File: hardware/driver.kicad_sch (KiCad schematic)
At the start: 33 parts, among them U4 EPC2152, U5 EPC2152, U6 INA181A2IDBVT, U7 INA181A2IDBVT, U8 EPC2152, U9 INA181A2IDBVT

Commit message: some layout
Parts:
- gave numbers to parts that had none: 12
- renumbered C22 to C42, C23 to C43, C24 to C44, C25 to C45, C26 to C46, C27 to C47, C28 to C48, C29 to C49, C30 to C50, R11 to R15, R12 to R16, R13 to R17, R14 to R18, R15 to R19, R16 to R23

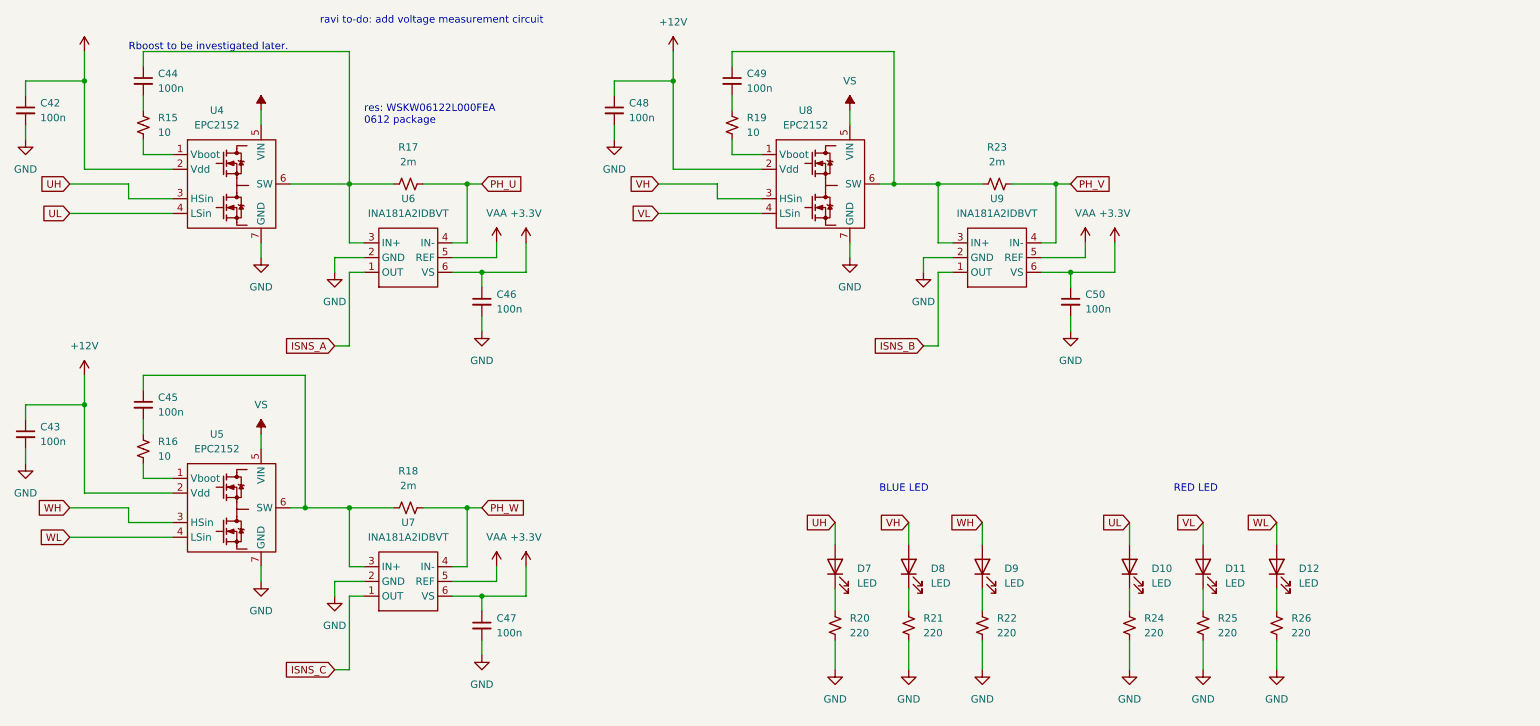
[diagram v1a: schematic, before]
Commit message: Simplified sensing, added some power layout.
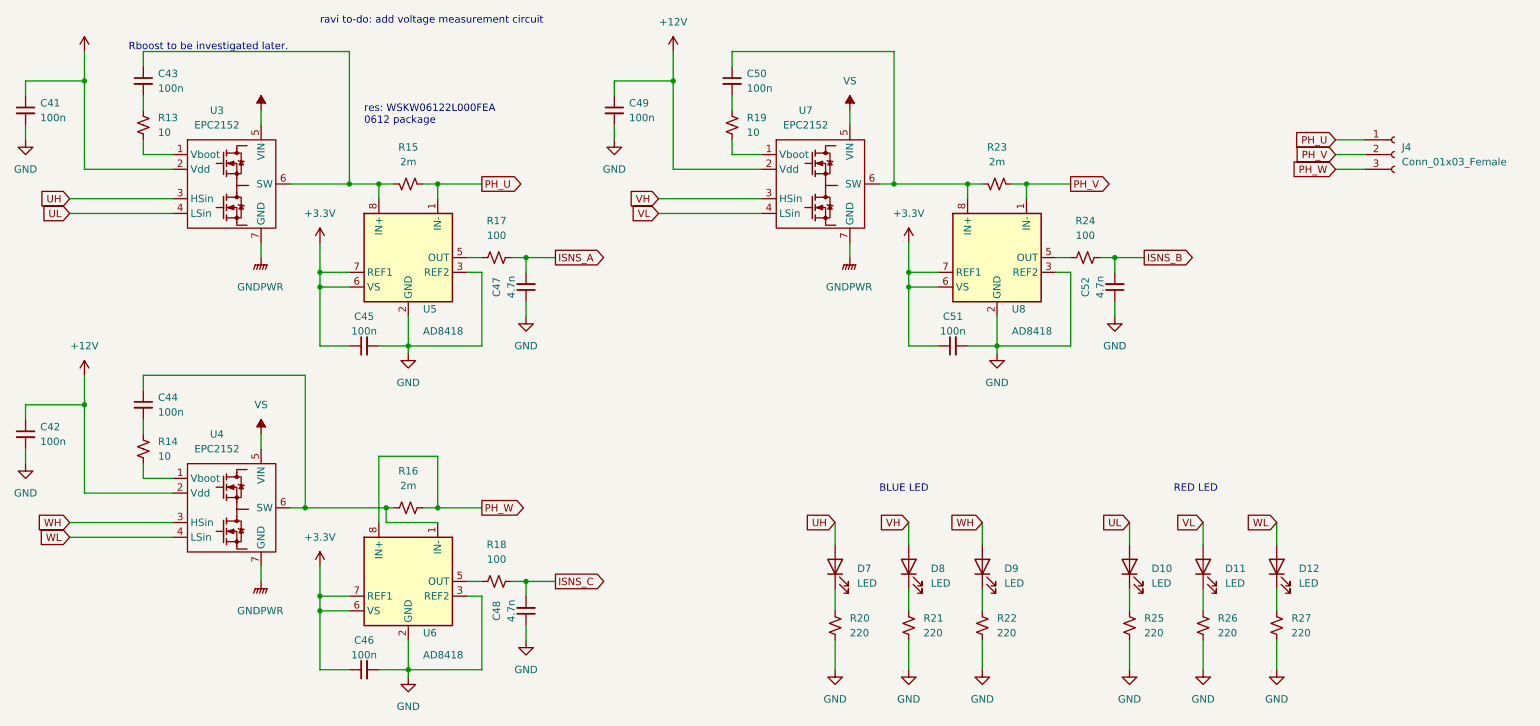
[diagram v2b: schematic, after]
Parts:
- removed C50: 100n, Capacitor_SMD:C_0805_2012Metric_Pad1.18x1.45mm_HandSolder, symbol Device:C_Small
- removed U6, U7, U9: INA181A2IDBVT, Package_TO_SOT_SMD:SOT-23-6_Handsoldering, symbol INA181A2IDBVT:INA181A2IDBVT
- added C45, C51: 100n, Capacitor_SMD:C_0805_2012Metric_Pad1.18x1.45mm_HandSolder, symbol Device:C_Small
- added C48, C52: 4.7n, Capacitor_SMD:C_0805_2012Metric_Pad1.18x1.45mm_HandSolder, symbol Device:C_Small
- added J4: Conn_01x03_Female, SnapEDA Library:1716090000, symbol Connector:Conn_01x03_Female
- added R17, R18, R24: 100, Resistor_SMD:R_0805_2012Metric, symbol Device:R_Small_US
- added U5, U6, U8: AD8418, Package_SO:MSOP-8-1EP_3x3mm_P0.65mm_EP1.68x1.88mm, symbol Amplifier_Current:AD8418
- C47: value 100n -> 4.7n
- D10, D11, D12, D7, D8, D9: footprint (none) -> LED_SMD:LED_0805_2012Metric
- renumbered C42 to C41, C43 to C42, C44 to C43, C45 to C44, C48 to C49, C49 to C50, R15 to R13, R16 to R14, R17 to R15, R18 to R16, R24 to R25, R25 to R26, R26 to R27, U4 to U3, U5 to U4, U8 to U7
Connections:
- net +3V3: now also C45.1, C51.1, U5.6 (VS), U5.7 (REF1), U6.6 (VS), U6.7 (REF1), U8.6 (VS), U8.7 (REF1); no longer C47.1
- net GND: now also C47.1, C45.2, C48.1, C51.2, C52.1, U5.2 (GND), U5.3 (REF2), U6.2 (GND), U6.3 (REF2), U8.2 (GND), U8.3 (REF2); no longer C47.2, U3.7 (GND), U4.7 (GND), U7.7 (GND)
- net ISNS_A: now also C47.2, R17.2
- net ISNS_B: now also C52.2, R24.2
- net ISNS_C: now also C48.2, R18.2
- net PH_U: now also R15.1, J4.1 (Pin_1), U5.1 (IN-); no longer R15.2
- net PH_V: now also R23.1, J4.2 (Pin_2), U8.1 (IN-); no longer R23.2
- net PH_W: now also J4.3 (Pin_3), U6.8 (IN+)
- net at C50.1, U7.6 (SW): now also R23.2, U8.8 (IN+); no longer R23.1
- net at C44.1, R16.1, U4.6 (SW): now also U6.1 (IN-)
- net at C43.1, U3.6 (SW): now also R15.2, U5.8 (IN+); no longer R15.1
- new net: R24.1, U8.5 (OUT)
- new net: R18.1, U6.5 (OUT)
- new net: R17.1, U5.5 (OUT)
- new net GNDPWR: U3.7 (GND), U4.7 (GND), U7.7 (GND)
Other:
- moved on the sheet: R15, R23
